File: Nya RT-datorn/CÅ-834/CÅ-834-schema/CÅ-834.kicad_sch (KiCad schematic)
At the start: 13 parts, among them IC1 74LS00, IC2 74LS244, IC3 74LS244, IC4 74LS245, IC5 74LS138, IC6 74LS138, IC7 74LS138, IC8 6116/2716, J1 A-B select, P1 RT-bus

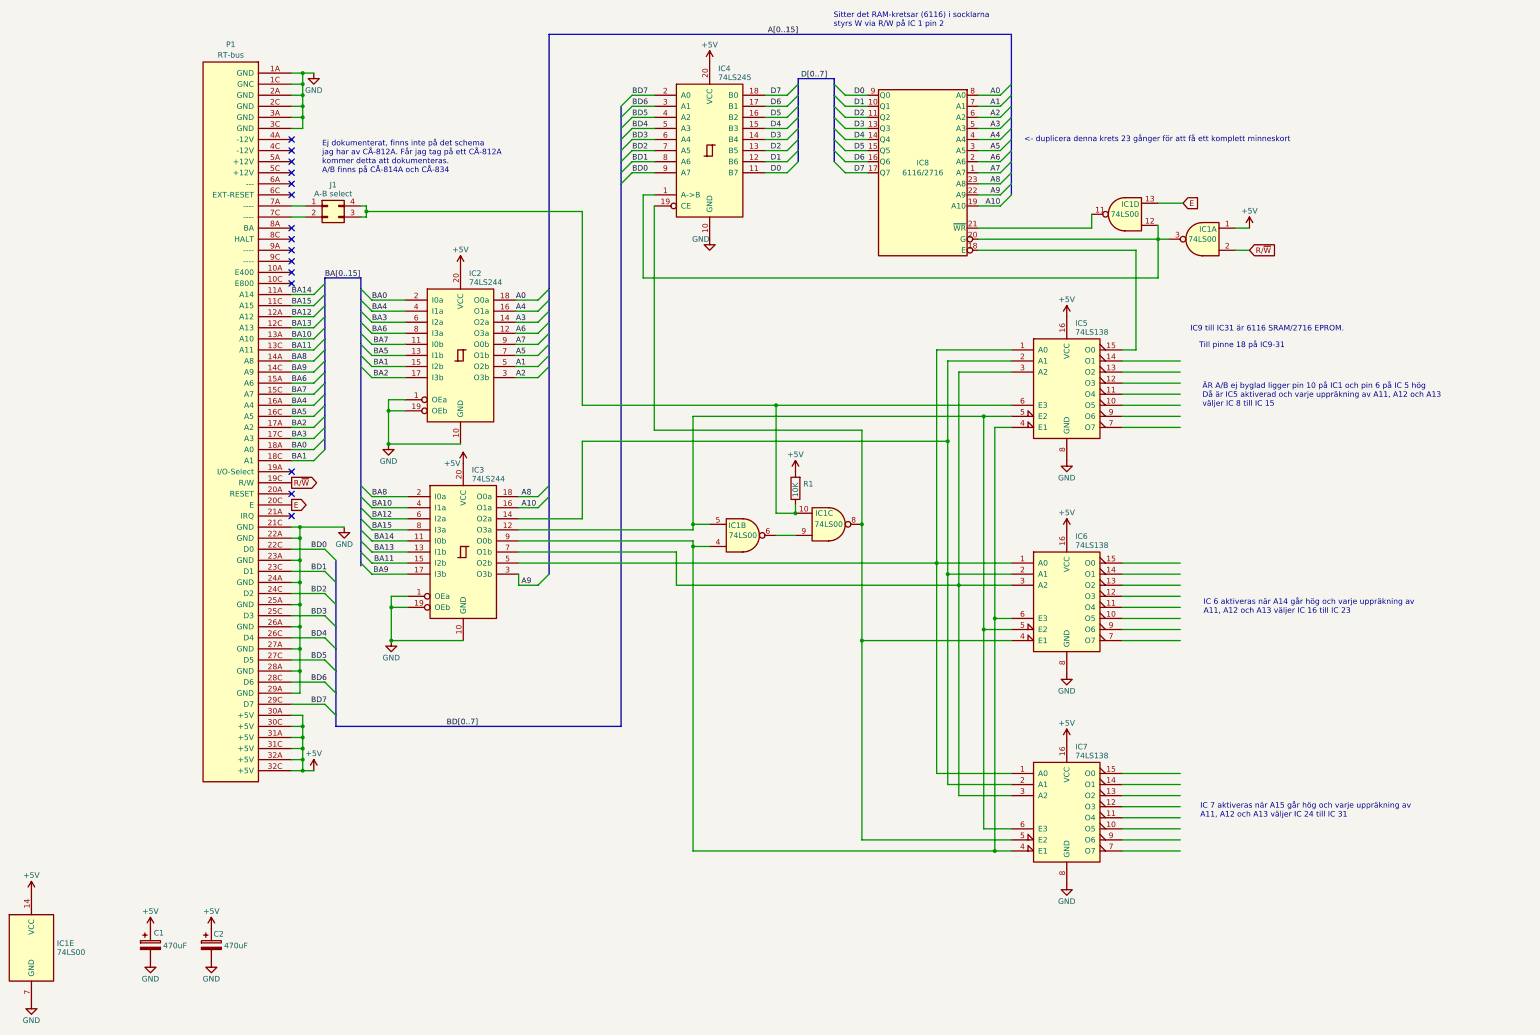
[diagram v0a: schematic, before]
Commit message: Uppdaterade schema CÅ-814A
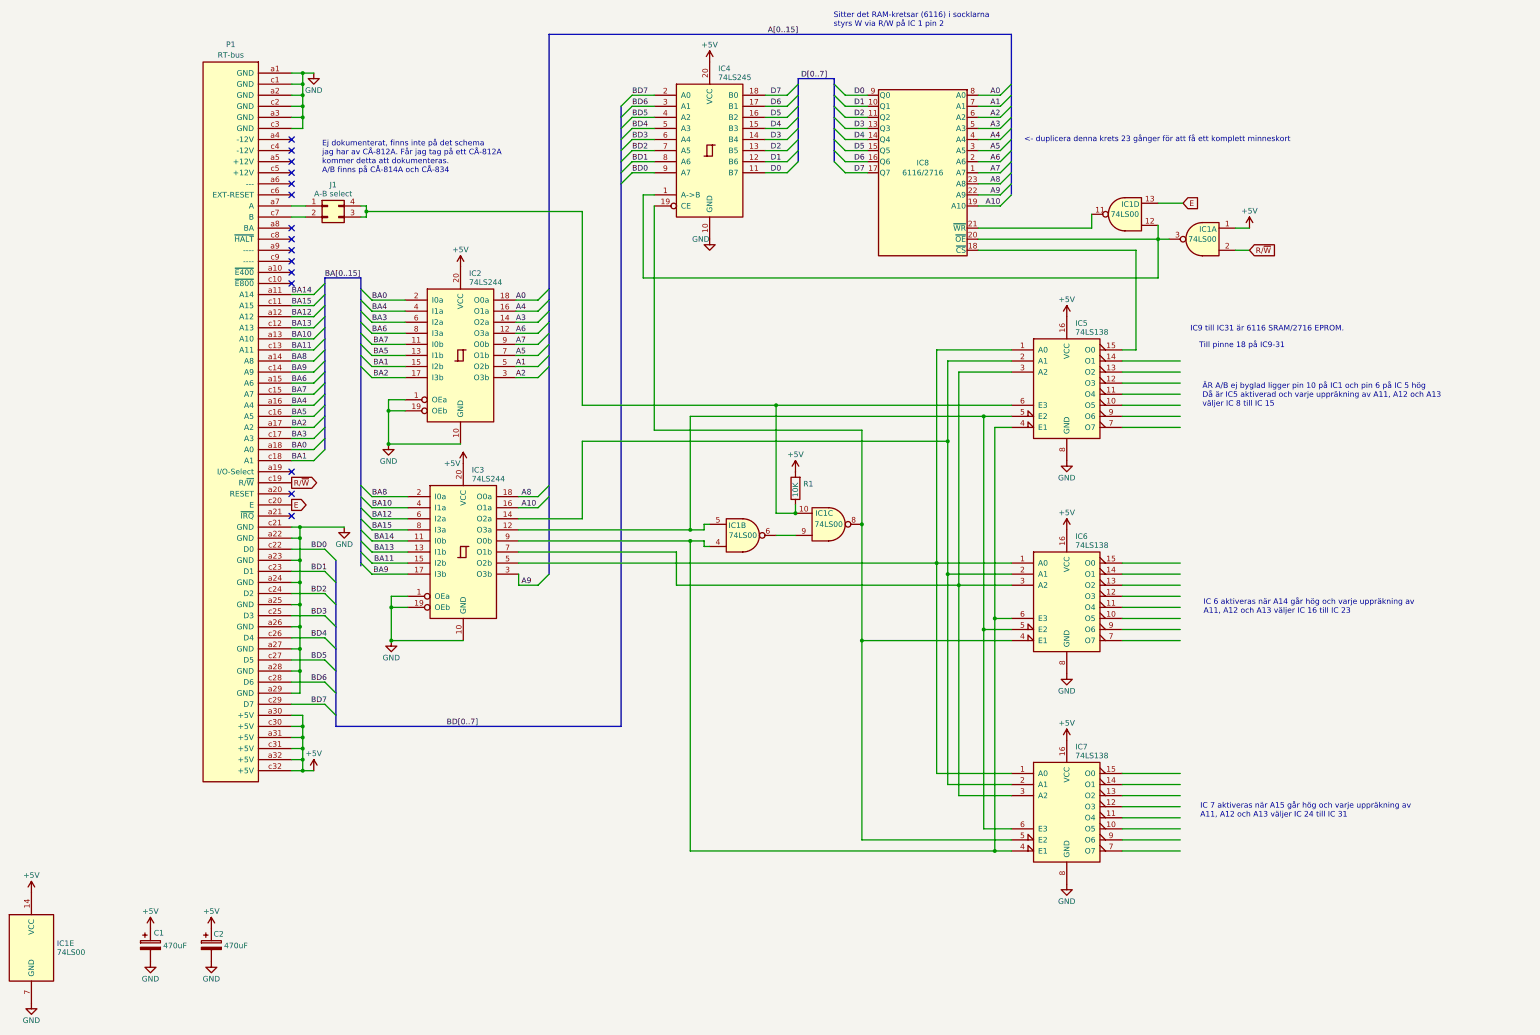
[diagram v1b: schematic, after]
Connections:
- net +5V: now also P1.a30 (+5V), P1.a31 (+5V), P1.a32 (+5V), P1.c30 (+5V), P1.c31 (+5V), P1.c32 (+5V); no longer P1.30A (+5V), P1.30C (+5V), P1.31A (+5V), P1.31C (+5V), P1.32A (+5V), P1.32C (+5V)
- net BA0: now also P1.a18 (A0); no longer P1.18A (A0)
- net BA1: now also P1.c18 (A1); no longer P1.18C (A1)
- net BA10: now also P1.a13 (A10); no longer P1.13A (A10)
- net BA11: now also P1.c13 (A11); no longer P1.13C (A11)
- net BA12: now also P1.a12 (A12); no longer P1.12A (A12)
- net BA13: now also P1.c12 (A13); no longer P1.12C (A13)
- net BA14: now also P1.a11 (A14); no longer P1.11A (A14)
- net BA15: now also P1.c11 (A15); no longer P1.11C (A15)
- net BA2: now also P1.a17 (A2); no longer P1.17A (A2)
- net BA3: now also P1.c17 (A3); no longer P1.17C (A3)
- net BA4: now also P1.a16 (A4); no longer P1.16A (A4)
- net BA5: now also P1.c16 (A5); no longer P1.16C (A5)
- net BA6: now also P1.a15 (A6); no longer P1.15A (A6)
- net BA7: now also P1.c15 (A7); no longer P1.15C (A7)
- net BA8: now also P1.a14 (A8); no longer P1.14A (A8)
- net BA9: now also P1.c14 (A9); no longer P1.14C (A9)
- net BD0: now also P1.c22 (D0); no longer P1.22C (D0)
- net BD1: now also P1.c23 (D1); no longer P1.23C (D1)
- net BD2: now also P1.c24 (D2); no longer P1.24C (D2)
- net BD3: now also P1.c25 (D3); no longer P1.25C (D3)
- net BD4: now also P1.c26 (D4); no longer P1.26C (D4)
- net BD5: now also P1.c27 (D5); no longer P1.27C (D5)
- net BD6: now also P1.c28 (D6); no longer P1.28C (D6)
- net BD7: now also P1.c29 (D7); no longer P1.29C (D7)
- net E: now also P1.c20 (E); no longer P1.20C (E)
- net GND: now also P1.a1 (GND), P1.a2 (GND), P1.a22 (GND), P1.a23 (GND), P1.a24 (GND), P1.a25 (GND), P1.a26 (GND), P1.a27 (GND), P1.a28 (GND), P1.a29 (GND), P1.a3 (GND), P1.c1 (GND), P1.c2 (GND), P1.c21 (GND), P1.c3 (GND); no longer P1.1A (GND), P1.1C (GNC), P1.21C (GND), P1.22A (GND), P1.23A (GND), P1.24A (GND), P1.25A (GND), P1.26A (GND), P1.27A (GND), P1.28A (GND), P1.29A (GND), P1.2A (GND), P1.2C (GND), P1.3A (GND), P1.3C (GND)
- net R/~{W}: now also P1.c19 (R/~{W}); no longer P1.19C (R/W)
- net at J1.1 (Pin_1): now also P1.a7 (A); no longer P1.7A (----)
- net at J1.2 (Pin_2): now also P1.c7 (B); no longer P1.7C (----)
